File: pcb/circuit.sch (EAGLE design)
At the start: 150 parts, among them IC1 MCP73833-AMI/UN-ND, IC2 MCP3423, IC3 MCP1612-ADJI/MS, IC4 WE-TVS, IC5 ATWINC1510-MR210PB1952-ND, IC6 RN4870, IC7 MAX3378EEUD, IC8 ATSAML22N18A, J1 USB2-MICRO, J10 2.5MM-AUDIO-JACK-MONO, J11 2.5MM-AUDIO-JACK-MONO, J12 22-05-7028-02, J2 2.5MM-AUDIO-JACK-MONO, J3 2.5MM-AUDIO-JACK-MONO, J4 2.5MM-AUDIO-JACK-MONO, J5 2.5MM-AUDIO-JACK-MONO, J6 2.5MM-AUDIO-JACK-MONO, J7 2.5MM-AUDIO-JACK-MONO, J8 2.5MM-AUDIO-JACK-MONO, J9 2.5MM-AUDIO-JACK-MONO, Q1 32kHz, T1 PMOS, T10 NMOSSOT323, T11 NMOSSOT323, T12 NMOSSOT323, T13 NMOSSOT323, T2 PMOS, T3 NMOSSOT323, T4 NMOSSOT323, T5 NMOSSOT323, T6 NMOSSOT323, T7 NMOSSOT323, T8 NMOSSOT323, T9 NMOSSOT323, X1 LI-ION_BATHOL2, X2 B3S-1000, X3 MOLEX_1MM_FPC, X4 IGRID-20

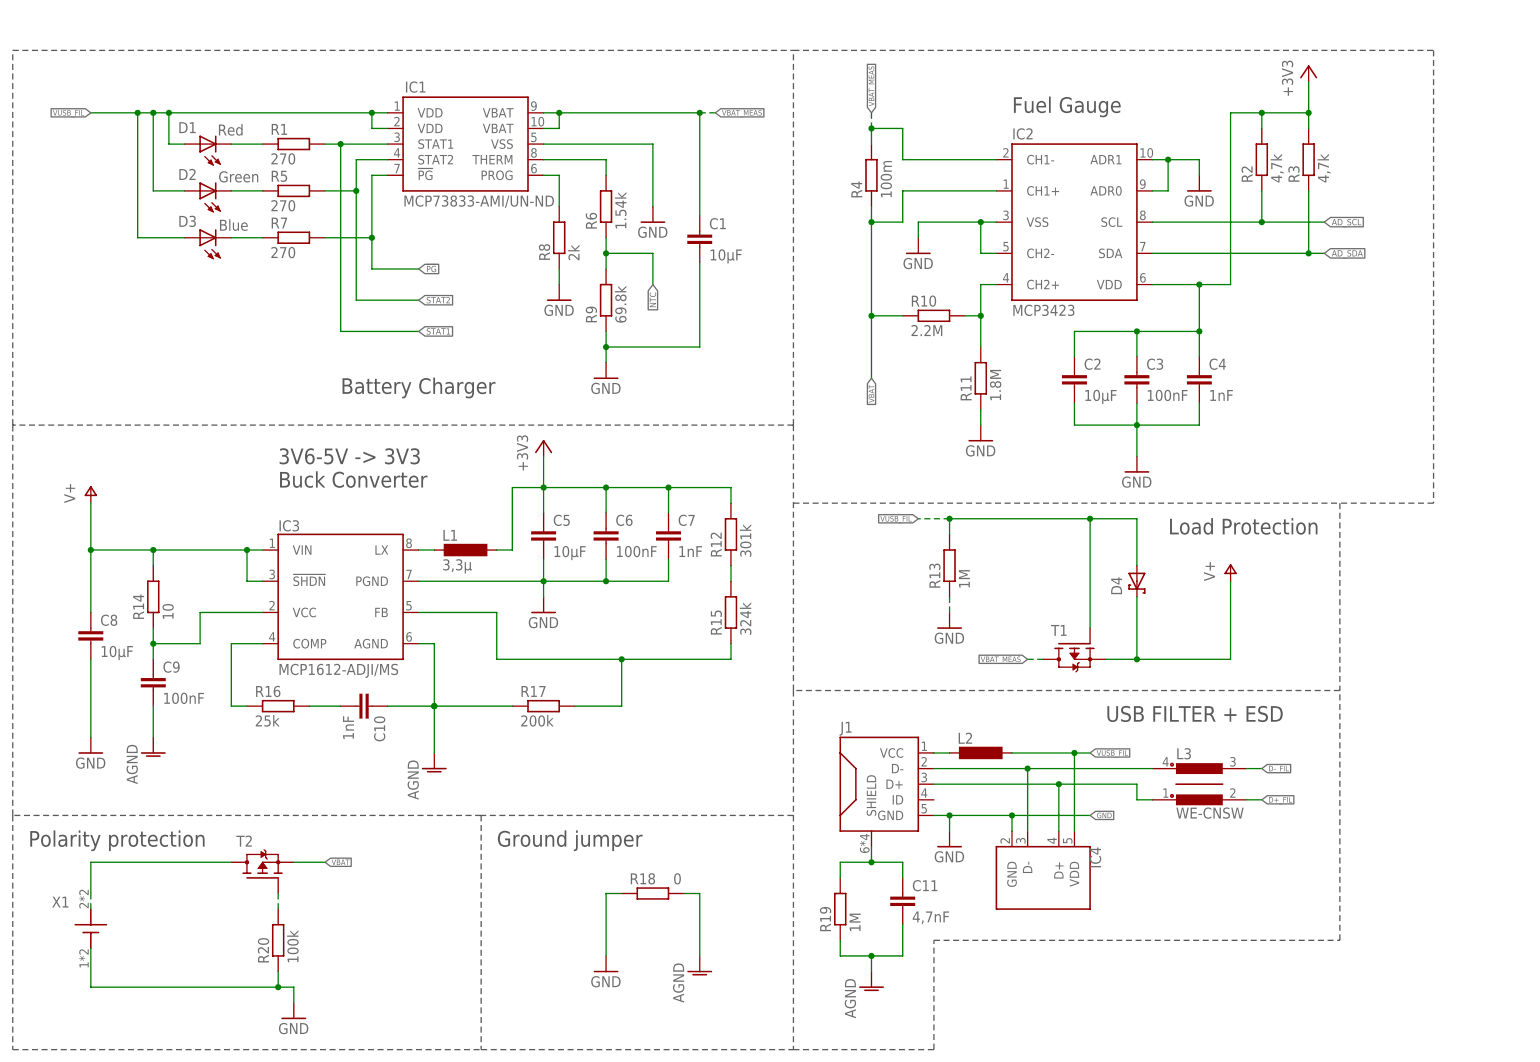
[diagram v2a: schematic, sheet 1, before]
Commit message: Board dimension created
-reworked schematics
-added PCB for battery-holder
-added PCB for UI
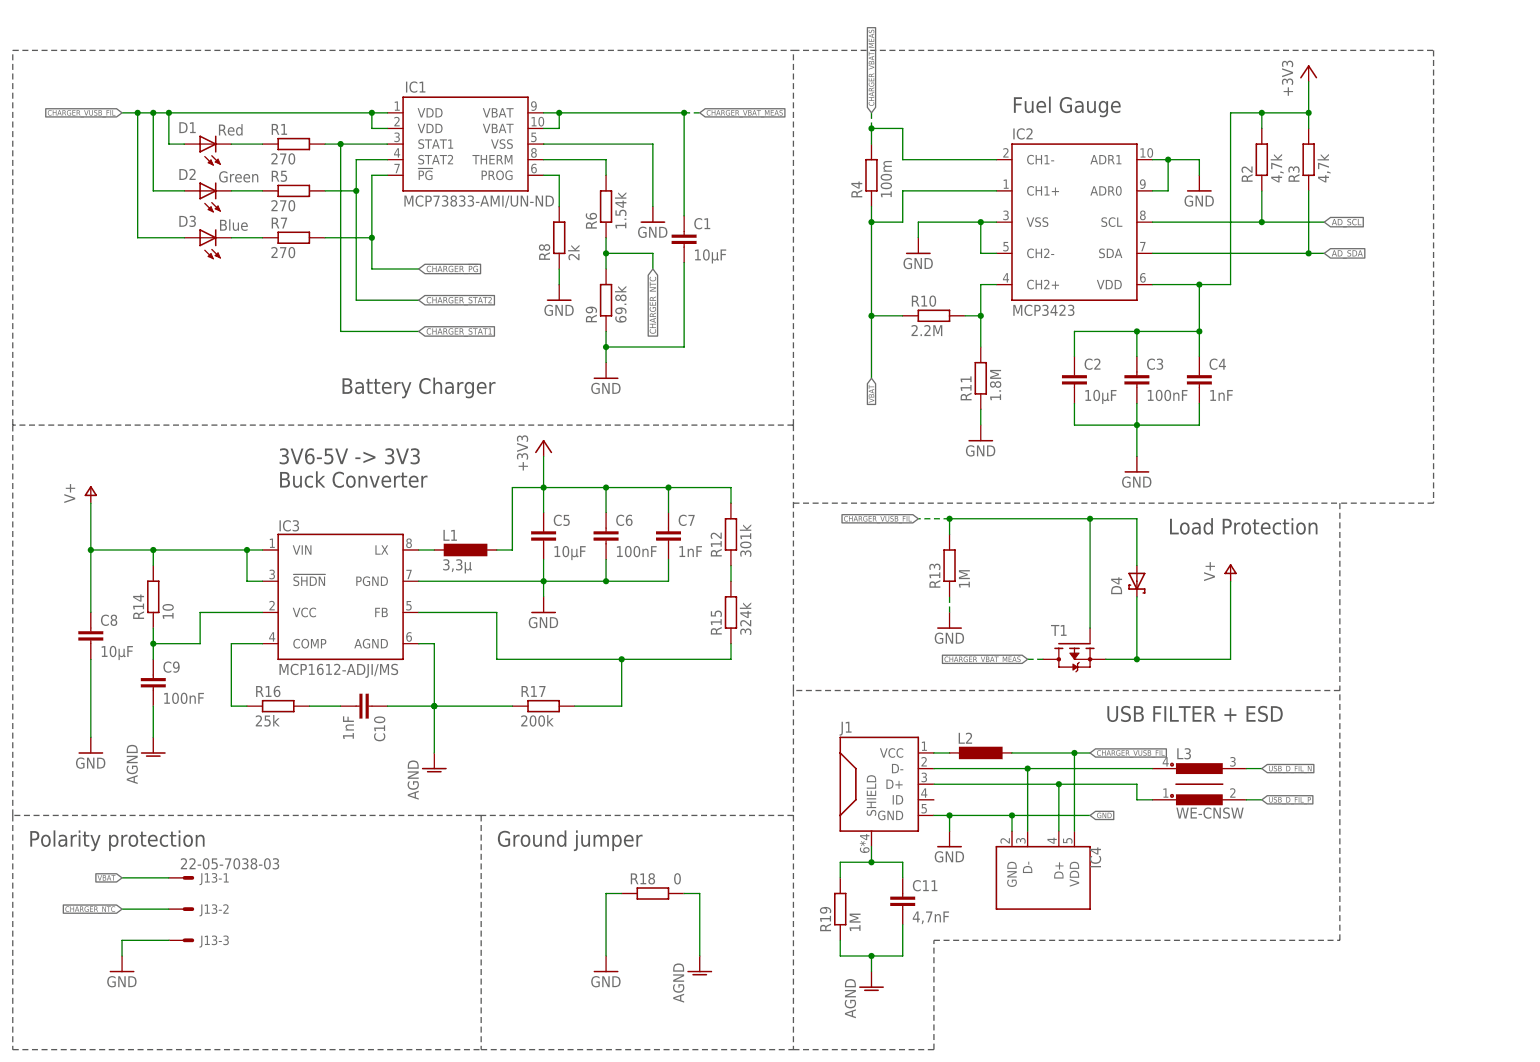
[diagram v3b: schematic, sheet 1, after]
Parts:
- removed C22: 100nF, rcl:C-EUC0603
- removed R20: 100k, rcl:R-EU_R0603
- removed T2: PMOS, thermo:PMOS
- removed X1: LI-ION_BATHOL2, thermo:LI-ION_BATHOL2
- added J13: 22-05-7038-03, con-molex:22-05-7038-03
- IC1: device Thermo_Library:MCP73833-AMI/UN-ND -> thermo:MCP73833-AMI/UN-ND; OC_MOUSER 579-MCP73833T-AMI/UN -> (none)
- IC2: OC_MOUSER 579-MCP3423-E/UN -> (none)
- IC3: OC_MOUSER 579-MCP1612T-ADJI/MS -> (none)
- IC5: device Thermo_Library:ATWINC1510-MR210PB1952-ND -> thermo:ATWINC1510-MR210PB1952-ND; OC_MOUSER 556-1510MR210UB1140 -> (none)
- IC6: device Thermo_Library:RN4870 -> thermo:RN4870; OC_MOUSER 579-RN4870-V/RM118 -> (none)
- IC8: device Thermo_Library:ATSAML22N18A -> thermo:ATSAML22N18A; OC_MOUSER 556-ATSAML22N18A-AUT -> (none)
- J11, J3, J5, J7, J9: value 2.5MM-AUDIO-JACK-MONO -> 2.5MM-AUDIO-JACK-MONONO_DRILL; device Thermo_Library:2.5MM-AUDIO-JACK-MONO -> thermo:2.5MM-AUDIO-JACK-MONONO_DRILL; OC_MOUSER 490-MJ-2523-SMT-TR -> (none)
- JP1, JP2, JP4, JP7: value (none) -> 4
- JP3: value (none) -> 3
- JP5, JP6: value (none) -> 2
- Q1: value 32kHz -> ECX-1210; device crystal:MC-405 -> thermo:ECX-1210; OC_FARNELL 2449409 -> (none)
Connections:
- net !PG! renamed CHARGER_!PG!
- net D+ renamed USB_D_P
- net D+_FIL renamed USB_D_FIL_P
- net D- renamed USB_D_N
- net D-_FIL renamed USB_D_FIL_N
- net FB renamed BUCK_FB
- net N$1 renamed AD_CH2+
- net N$12 renamed CHARGER_STAT1_LED
- net N$13 renamed BUCK_FB_R
- net N$14 renamed CHARGER_STAT2_LED
- net N$15 renamed CHARGER_!PG!_LED
- net N$16 renamed SENSOR_IN_9_DRAIN
- net N$19 renamed SENSOR_IN_0_DRAIN
- net N$2 renamed SENSOR_IN_5_DRAIN
- net N$20 renamed SENSOR_IN_1_DRAIN
- net N$21 renamed SENSOR_IN_2_DRAIN
- net N$22 renamed SENSOR_IN_3_DRAIN
- net N$24 renamed WIFI_WAKE_D
- net N$29 renamed WIFI_SPI_MISO_D
- net N$3 renamed SENSOR_IN_6_DRAIN
- net N$30 renamed WIFI_SPI_SSN_D
- net N$32 renamed OLED_EN_DRAIN
- net N$37 renamed USB_SHIELD
- net N$4 renamed SENSOR_IN_7_DRAIN
- net N$45 renamed WIFI_SPI_CFG
- net N$48 renamed WIFI_1P3V_TP
- net N$5 renamed SENSOR_IN_8_DRAIN
- net N$57 renamed BT_!RESET!
- net N$6 renamed SENSOR_IN_4_DRAIN
- net N$7 renamed !RESET!_B
- net N$8 renamed BUCK_LX
- net PROG renamed CHARGER_PROG
- net STAT1 renamed CHARGER_STAT1
- net STAT2 renamed CHARGER_STAT2
- net THERM renamed CHARGER_THERM
- net V+ renamed BUCK_V+
- net VBAT_MEAS renamed CHARGER_VBAT_MEAS
- net VUSB renamed USB_VCC
- net VUSB_FIL renamed CHARGER_VUSB_FIL
- removed net N$17: R20.2, T2.G
- removed net N$23: C18.1, C19.1, C20.1, L5.1
- removed net NTC: R6.1, R9.2
- removed net RESET: C22.1
- removed net SOF_NC: IC8.PA23
- new net +3V3_ANA: C18.1, C19.1, C20.1, IC8.VDDANA@1, IC8.VDDANA@2, L5.1
- new net CHARGER_NTC: J13-2.S, R6.1, R9.2
- net +3V3: no longer IC8.VDDANA@1, IC8.VDDANA@2
- net GND: now also J13-3.S; no longer C22.2, R20.1, X1.VBAT-
- net VBAT: now also J13-1.S; no longer T2.S
- net VIN: no longer T2.D, X1.VBAT+
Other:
- moved on the sheet: C1

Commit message: Power Unit
- placed power devices
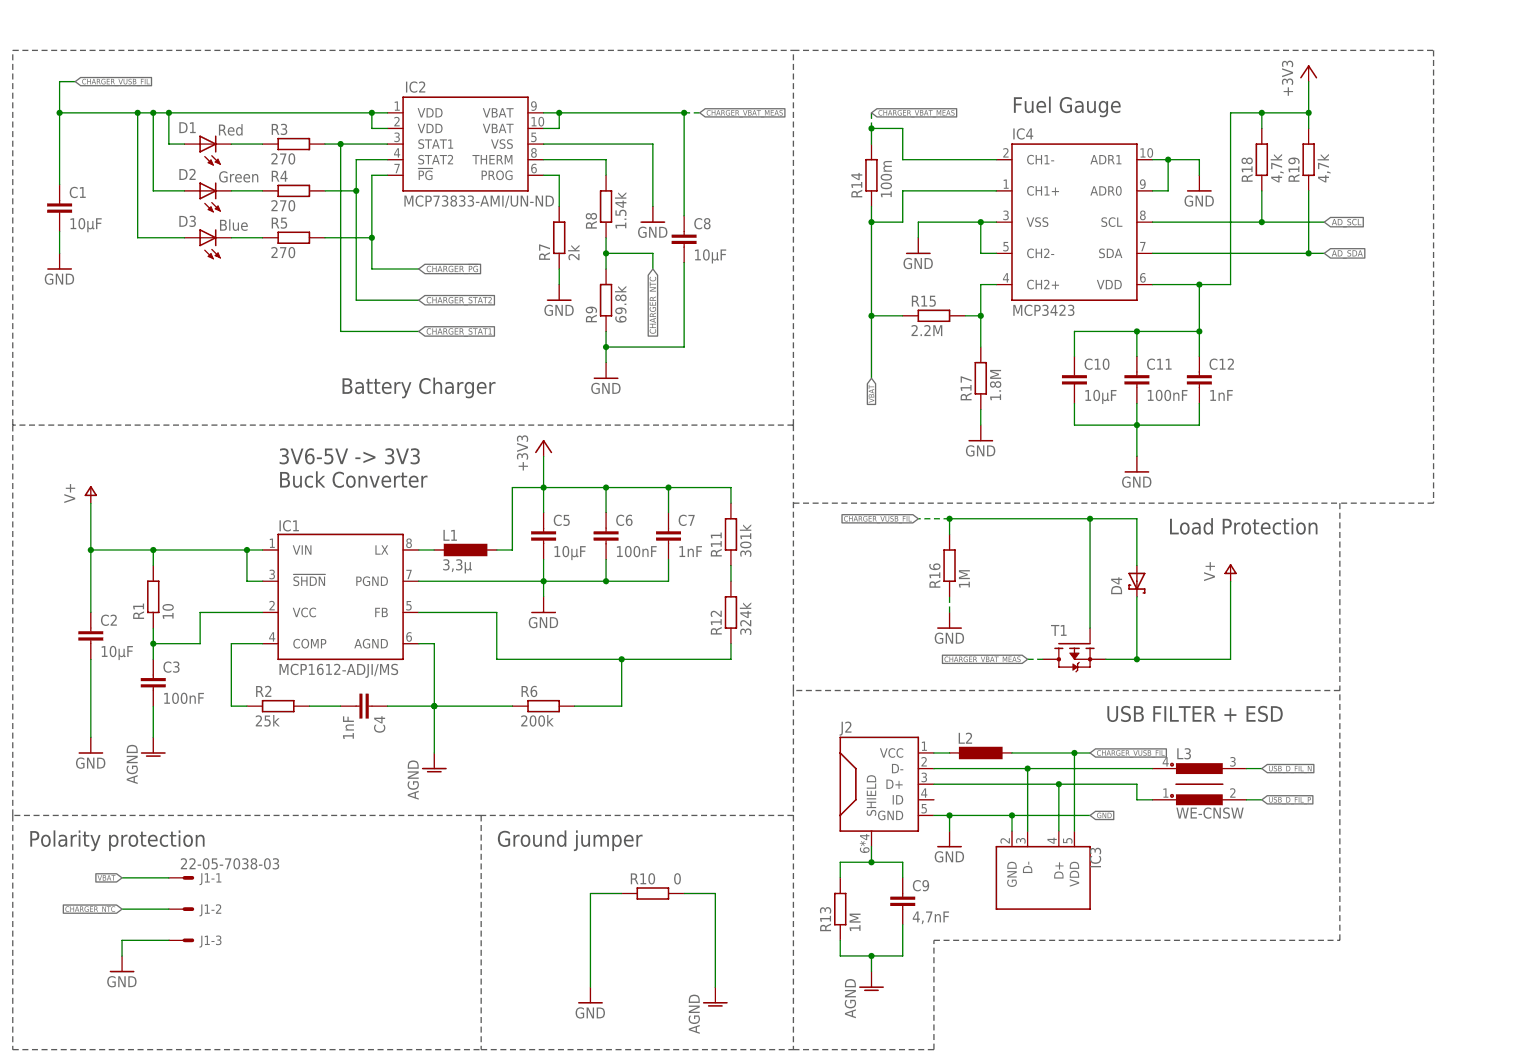
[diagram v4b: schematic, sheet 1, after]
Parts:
- removed R58: 1M, rcl:R-EU_R0603
- removed T13: NMOSSOT323, Thermo_Library:NMOSSOT323
- removed X4: IGRID-20, thermo:IGRID-20
- added C22: 10µF, rcl:C-EUC0805
- added R20: 330, rcl:R-EU_R0603
- added T2: NMOSSOT323, Thermo_Library:NMOSSOT323
- added X1: B3S-1000, Thermo_Library:B3S-1000
- C10, C27: value 1nF -> 10µF; device rcl:C-EUC0603 -> rcl:C-EUC0805; OC_MOUSER 80-C0603C102K3R -> 81-GRM21BR61E106KA3L
- C11: value 4,7nF -> 100nF; OC_MOUSER 80-C0603C472K3R -> 581-06033C104KAT2A
- C12, C28: value 100nF -> 1nF; OC_MOUSER 581-06033C104KAT2A -> 80-C0603C102K3R
- C17, C18: value 10µF -> 100nF; device rcl:C-EUC0805 -> rcl:C-EUC0603; OC_MOUSER 81-GRM21BR61E106KA3L -> 581-06033C104KAT2A
- C20, C32, C37: value 100nF -> 1µF; OC_MOUSER 581-06033C104KAT2A -> 810-CGA3E1X7R1E105AC
- C21, C34: value 100nF -> 10µF; device rcl:C-EUC0603 -> rcl:C-EUC0805; OC_MOUSER 581-06033C104KAT2A -> 81-GRM21BR61E106KA3L
- C23, C33: value 1µF -> 100nF; OC_MOUSER 810-CGA3E1X7R1E105AC -> 581-06033C104KAT2A
- C24, C25: value 22pF -> 100nF; OC_MOUSER 581-02013A220FAT2A -> 581-06033C104KAT2A
- C29: value 10µF -> 1µF; device rcl:C-EUC0805 -> rcl:C-EUC0603; OC_MOUSER 81-GRM21BR61E106KA3L -> 810-CGA3E1X7R1E105AC
- C30: value 10µF -> 1nF; device rcl:C-EUC0805 -> rcl:C-EUC0603; OC_MOUSER 81-GRM21BR61E106KA3L -> 80-C0603C102K3R
- C31: value 1nF -> 100nF; OC_MOUSER 80-C0603C102K3R -> 581-06033C104KAT2A
- C35, C36: value 1µF -> 22pF; OC_MOUSER 810-CGA3E1X7R1E105AC -> 581-02013A220FAT2A
- C9: value 100nF -> 4,7nF; OC_MOUSER 581-06033C104KAT2A -> 80-C0603C472K3R
- IC1: value MCP73833-AMI/UN-ND -> MCP1612-ADJI/MS; device thermo:MCP73833-AMI/UN-ND -> thermo:MCP1612-ADJI/MS
- IC2: value MCP3423 -> MCP73833-AMI/UN-ND; device thermo:MCP3423 -> thermo:MCP73833-AMI/UN-ND
- IC3: value MCP1612-ADJI/MS -> WE-TVS; device thermo:MCP1612-ADJI/MS -> thermo:WE-TVS; OC_MOUSER (none) -> 710-824011
- IC4: value WE-TVS -> MCP3423; device thermo:WE-TVS -> thermo:MCP3423; OC_MOUSER 710-824011 -> (none)
- IC6: value RN4870 -> MAX3378EEUD; device thermo:RN4870 -> thermo:MAX3378EEUD; OC_MOUSER (none) -> 700-MAX3378EEUD
- IC7: value MAX3378EEUD -> RN4870; device thermo:MAX3378EEUD -> thermo:RN4870; OC_MOUSER 700-MAX3378EEUD -> (none)
- J1: value USB2-MICRO -> 22-05-7038-03; device thermo:USB2-MICRO -> con-molex:22-05-7038-03; OC_MOUSER 649-10104110-0001LF -> (none)
- J10: value 2.5MM-AUDIO-JACK-MONO -> 2.5MM-AUDIO-JACK-MONONO_DRILL; device Thermo_Library:2.5MM-AUDIO-JACK-MONO -> thermo:2.5MM-AUDIO-JACK-MONONO_DRILL; OC_MOUSER 490-MJ-2523-SMT-TR -> (none)
- J12: value 22-05-7028-02 -> 2.5MM-AUDIO-JACK-MONONO_DRILL; device con-molex:22-05-7028-02 -> thermo:2.5MM-AUDIO-JACK-MONONO_DRILL; OC_MOUSER 538-22-05-7028 -> (none)
- J13: value 22-05-7038-03 -> 2.5MM-AUDIO-JACK-MONONO_DRILL; device con-molex:22-05-7038-03 -> thermo:2.5MM-AUDIO-JACK-MONONO_DRILL
- J2: value 2.5MM-AUDIO-JACK-MONO -> USB2-MICRO; device Thermo_Library:2.5MM-AUDIO-JACK-MONO -> thermo:USB2-MICRO; OC_MOUSER 490-MJ-2523-SMT-TR -> 649-10104110-0001LF
- J3, J5, J7: value 2.5MM-AUDIO-JACK-MONONO_DRILL -> 2.5MM-AUDIO-JACK-MONO; device thermo:2.5MM-AUDIO-JACK-MONONO_DRILL -> Thermo_Library:2.5MM-AUDIO-JACK-MONO; OC_MOUSER (none) -> 490-MJ-2523-SMT-TR
- J8: value 2.5MM-AUDIO-JACK-MONO -> 22-05-7028-02; device Thermo_Library:2.5MM-AUDIO-JACK-MONO -> con-molex:22-05-7028-02; OC_MOUSER 490-MJ-2523-SMT-TR -> 538-22-05-7028
- JP3: value 3 -> 2; device jumper:JP2E -> jumper:JP1E; OC_FARNELL 710-61300311121 -> (none); OC_MOUSER (none) -> 855-M20-9990246
- JP4: value 4 -> 2; device jumper:JP4E -> jumper:JP1E; OC_MOUSER 855-M20-9770446 -> 855-M20-9990246
- JP5: value 2 -> 3; device jumper:JP1E -> jumper:JP2E; OC_FARNELL (none) -> 710-61300311121; OC_MOUSER 855-M20-9990246 -> (none)
- JP6: value 2 -> 4; device jumper:JP1E -> jumper:JP4E; OC_MOUSER 855-M20-9990246 -> 855-M20-9770446
- L4: value 10µH -> L-0603; device Thermo_Library:L-1210 -> Thermo_Library:L-0603; OC_MOUSER 871-B82422H1103K -> 81-BLM18EG221SN1D
- L5: value L-0603 -> 10µH; device Thermo_Library:L-0603 -> Thermo_Library:L-1210; OC_MOUSER 81-BLM18EG221SN1D -> 871-B82422H1103K
- R1: value 270 -> 10; OC_MOUSER 652-CR0603FX-2700ELF -> 603-RC0603FR-0710RL
- R10: value 2.2M -> 0; OC_MOUSER 603-RC0603FR-072M2L -> 603-RC0603JR-070RL
- R11: value 1.8M -> 301k; OC_MOUSER 603-RC0603FR-071M8L -> 603-RC0603FR-07301KL
- R12: value 301k -> 324k; OC_MOUSER 603-RC0603FR-07301KL -> 603-RC0603FR-07324KL
- R14: value 10 -> 100m; device rcl:R-EU_R0603 -> rcl:R-EU_R5025; OC_MOUSER 603-RC0603FR-0710RL -> 652-CRM2010FXR100ELF
- R15: value 324k -> 2.2M; OC_MOUSER 603-RC0603FR-07324KL -> 603-RC0603FR-072M2L
- R16: value 25k -> 1M; device rcl:R-EU_R0805 -> rcl:R-EU_R0603; OC_MOUSER 279-CPF0805B25KE1 -> 603-RC0603FR-071ML
- R17: value 200k -> 1.8M; OC_MOUSER 603-RC0603FR-07200KL -> 603-RC0603FR-071M8L
- R18: value 0 -> 4,7k; OC_MOUSER 603-RC0603JR-070RL -> 603-RC0603FR-074K7L
- R19: value 1M -> 4,7k; OC_MOUSER 603-RC0603FR-071ML -> (none)
- R2: value 4,7k -> 25k; device rcl:R-EU_R0603 -> rcl:R-EU_R0805; OC_MOUSER 603-RC0603FR-074K7L -> 279-CPF0805B25KE1
- R21, R22: value 0 -> 1M; OC_MOUSER 603-RC0603JR-070RL -> 603-RC0603FR-071ML
- R23: value 0 -> 10k; OC_MOUSER 603-RC0603JR-070RL -> 603-RC0603FR-0710KL
- R26, R31: value 1M -> 0; OC_MOUSER 603-RC0603FR-071ML -> 603-RC0603JR-070RL
- R3: value 4,7k -> 270; OC_MOUSER (none) -> 652-CR0603FX-2700ELF
- R32: value 4,7k -> 0; OC_MOUSER (none) -> 603-RC0603JR-070RL
- R36: value 10k -> 4,7k; OC_MOUSER 603-RC0603FR-0710KL -> (none)
- R37: value 330 -> 1M; OC_MOUSER 603-RC0603FR-07330RL -> 603-RC0603FR-071ML
- R4: value 100m -> 270; device rcl:R-EU_R5025 -> rcl:R-EU_R0603; OC_FARNELL (none) -> 2447144; OC_MOUSER 652-CRM2010FXR100ELF -> (none)
- R43, R44, R45, R46, R47: value 4.7k 0.1% -> 1M; OC_MOUSER 279-CPF0603B4K7E1 -> 603-RC0603FR-071ML
- R48, R49, R50, R51, R52: value 1M -> 4.7k 0.1%; OC_MOUSER 603-RC0603FR-071ML -> 279-CPF0603B4K7E1
- R6: value 1.54k -> 200k; OC_MOUSER 660-RK73H1JTTD1541F -> 603-RC0603FR-07200KL
- R7: value 270 -> 2k; OC_FARNELL 2447144 -> (none); OC_MOUSER (none) -> 652-CR0603-FX-2001LF
- R8: value 2k -> 1.54k; OC_MOUSER 652-CR0603-FX-2001LF -> 660-RK73H1JTTD1541F
- X2: value B3S-1000 -> MOLEX_1MM_FPC; device Thermo_Library:B3S-1000 -> thermo:MOLEX_1MM_FPC; OC_MOUSER 653-B3S-1000 -> (none)
- X3: value MOLEX_1MM_FPC -> IGRID-20; device thermo:MOLEX_1MM_FPC -> thermo:IGRID-20; OC_MOUSER (none) -> 538-501645-2020
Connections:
- net !OLED_RESET: now also X3.16; no longer X4.16
- net !OLED_SPI_CS: now also X3.17; no longer X4.17
- net !PG!_TRANS: now also IC6.I/OVL1; no longer IC7.I/OVL1
- net !RESET!: now also C15.1, R20.2, R23.1; no longer C37.1, R36.1, R37.2
- net !RESET!_B: now also R20.1, X1.S; no longer R37.1, X2.S
- net +3V3: now also C10.1, C11.1, C18.1, C19.1, C20.1, C21.1, C30.1, C33.1, IC4.VDD, IC6.VL, IC7.VBAT, IC7.VDD_IO@1, IC7.VDD_IO@2, L4.2, R11.2, R18.2, R19.2, R23.2, R34.2, R35.2, X2.1, X3.2; no longer C15.1, C2.1, C26.1, C28.1, C29.1, C3.1, C35.1, C4.1, IC2.VDD, IC6.VBAT, IC6.VDD_IO@1, IC6.VDD_IO@2, IC7.VL, J10.2, J11.2, J2.2, J3.2, J4.2, J5.2, J6.2, J7.2, J8.2, J9.2, L5.2, R12.2, R2.2, R26.2, R3.2, R31.2, R32.2, X3.1, X4.2
- net +3V3_ANA: now also C22.1, C23.1, C24.1, J10.2, J11.2, J12.2, J13.2, J3.2, J4.2, J5.2, J6.2, J7.2, J9.2, L4.1; no longer C18.1, C19.1, C20.1, L5.1
- net AD_CH2+: now also IC4.CH2+, R15.2, R17.2; no longer IC2.CH2+, R10.2, R11.2
- net AD_SCL: now also IC4.SCL, JP3.1, R18.1; no longer IC2.SCL, JP5.1, R2.1
- net AD_SDA: now also IC4.SDA, JP3.2, R19.1; no longer IC2.SDA, JP5.2, R3.1
- net AGND: now also C22.2, C23.2, C24.2, C25.2, C3.2, C4.1, IC1.AGND, R10.2, R13.1, R6.1, T2.S; no longer C10.1, C11.2, C18.2, C19.2, C20.2, C21.2, IC3.AGND, R17.1, R18.2, R19.1, T12.S
- net BT_!RESET!: now also C37.1, IC7.!RST!, R36.1; no longer C33.1, IC6.!RST!, R32.1
- net BT_LINK_DROP: now also IC7.P3_2; no longer IC6.P3_2
- net BT_MODE: now also IC7.P2_0/MODE, R35.1; no longer IC6.P2_0/MODE, R31.1
- net BT_PAIRING_KEY: now also IC7.P3_4; no longer IC6.P3_4
- net BT_RSSI_IND: now also IC7.P3_1; no longer IC6.P3_1
- net BT_RX_IND: now also IC7.P3_3; no longer IC6.P3_3
- net BT_STATUS_1: now also IC7.P1_1; no longer IC6.P1_1
- net BT_STATUS_2: now also IC7.P1_0; no longer IC6.P1_0
- net BT_TX_IND: now also IC7.P2_7/TX_IND; no longer IC6.P2_7/TX_IND
- net BT_UART_CTS: now also IC7.P0_0/CTS, JP6.2; no longer IC6.P0_0/CTS, JP4.2
- net BT_UART_RTS: now also IC7.P3_6/RTS, JP6.1; no longer IC6.P3_6/RTS, JP4.1
- net BT_UART_RX: now also IC7.UART_RX, JP6.4; no longer IC6.UART_RX, JP4.4
- net BT_UART_TX: now also IC7.UART_TX, JP6.3; no longer IC6.UART_TX, JP4.3
- net BUCK_FB: now also IC1.FB, R12.1, R6.2; no longer IC3.FB, R15.1, R17.2
- net BUCK_FB_R: now also R11.1, R12.2; no longer R12.1, R15.2
- net BUCK_LX: now also IC1.LX; no longer IC3.LX
- net BUCK_RC_C: now also C4.2, R2.2; no longer C10.2, R16.2
- net BUCK_RC_R: now also IC1.COMP, R2.1; no longer IC3.COMP, R16.1
- net BUCK_V+: now also C2.1, IC1.!SHDN!, IC1.VIN, R1.2; no longer C8.1, IC3.!SHDN!, IC3.VIN, R14.2
- net BUCK_VCC: now also C3.1, IC1.VCC, R1.1; no longer C9.1, IC3.VCC, R14.1
- net CHARGER_!PG!: now also IC2.!PG, IC6.I/OVCC1, R5.2; no longer IC1.!PG, IC7.I/OVCC1, R7.2
- net CHARGER_!PG!_LED: now also R5.1; no longer R7.1
- net CHARGER_NTC: now also J1-2.S, R8.1; no longer J13-2.S, R6.1
- net CHARGER_PROG: now also IC2.PROG, R7.2; no longer IC1.PROG, R8.2
- net CHARGER_STAT1: now also IC2.STAT1, IC6.I/OVCC3, R3.2; no longer IC1.STAT1, IC7.I/OVCC3, R1.2
- net CHARGER_STAT1_LED: now also R3.1; no longer R1.1
- net CHARGER_STAT2: now also IC2.STAT2, IC6.I/OVCC2, R4.2; no longer IC1.STAT2, IC7.I/OVCC2, R5.2
- net CHARGER_STAT2_LED: now also R4.1; no longer R5.1
- net CHARGER_THERM: now also IC2.THERM, R8.2; no longer IC1.THERM, R6.2
- net CHARGER_VBAT_MEAS: now also C8.1, IC2.VBAT@1, IC2.VBAT@2, IC4.CH1-, R14.2; no longer C1.1, IC1.VBAT@1, IC1.VBAT@2, IC2.CH1-, R4.2
- net CHARGER_VUSB_FIL: now also C1.1, C32.1, IC2.VDD@1, IC2.VDD@2, IC3.VDD, IC6.!TS!, IC6.I/OVCC4, IC6.VCC, R16.2; no longer C36.1, IC1.VDD@1, IC1.VDD@2, IC4.VDD, IC7.!TS!, IC7.I/OVCC4, IC7.VCC, R13.2
- net EXT_PWM_0: now also J8-1.S; no longer J12-1.S
- net EXT_PWM_1: now also J8-2.S; no longer J12-2.S
- net GND: now also C10.2, C11.2, C18.2, C19.2, C20.2, C21.2, IC1.PGND, IC3.GND, IC4.ADR0, IC4.ADR1, IC4.CH2-, IC4.VSS, IC6.GND, IC7.GND@1, IC7.GND@2, IC7.GND@3, IC7.GND@4, IC7.GND@5, IC7.GND@6, J1-3.S, J2.GND, R10.1, R16.1, R17.1, R21.1, R22.1, R37.1, R43.1, R44.1, R45.1, R46.1, R47.1, R7.1, T12.S, X1.P, X2.6; no longer C23.2, C24.2, C25.2, C3.2, C4.2, IC1.VSS, IC2.ADR0, IC2.ADR1, IC2.CH2-, IC3.PGND, IC4.GND, IC6.GND@1, IC6.GND@2, IC6.GND@3, IC6.GND@4, IC6.GND@5, IC6.GND@6, IC7.GND, J1.GND, J13-3.S, R11.1, R13.1, R18.1, R34.1, R35.1, R48.1, R49.1, R50.1, R51.1, R52.1, R58.1, R8.1, T13.S, X2.P, X3.6
- net OLED_D/C: now also X3.4; no longer X4.4
- net OLED_EN: now also R57.2, T12.G; no longer R58.2, T13.G
- net OLED_EN_DRAIN: now also T12.D, X3.1, X3.10, X3.11, X3.12, X3.13, X3.14, X3.19, X3.20, X3.5, X3.6; no longer T13.D, X4.1, X4.10, X4.11, X4.12, X4.13, X4.14, X4.19, X4.20, X4.5, X4.6
- net OLED_SPI_MOSI: now also X3.8; no longer X4.8
- net OLED_SPI_SCLK: now also X3.7; no longer X4.7
- net RES0: now also JP5.1; no longer JP3.1
- net RES1: now also JP5.2; no longer JP3.2
- net RES2: now also JP5.3; no longer JP3.3
- net SENSOR_EN_0: now also R37.2, T2.G; no longer R48.2, T3.G
- net SENSOR_EN_1: now also R43.2, T3.G; no longer R49.2, T5.G
- net SENSOR_EN_2: now also R44.2, T4.G; no longer R50.2, T7.G
- net SENSOR_EN_3: now also R45.2, T5.G; no longer R51.2, T9.G
- net SENSOR_EN_4: now also R46.2, T6.G; no longer R52.2, T11.G
- net SENSOR_EN_5: now also R47.2, T7.G; no longer R53.2, T4.G
- net SENSOR_EN_6: now also R53.2, T8.G; no longer R54.2, T6.G
- net SENSOR_EN_7: now also R54.2, T9.G; no longer R55.2, T8.G
- net SENSOR_EN_8: now also R55.2; no longer R56.2
- net SENSOR_EN_9: now also R56.2, T11.G; no longer R57.2, T12.G
- net SENSOR_INT_0: now also J3.3; no longer J2.3
- net SENSOR_INT_2: now also J5.3; no longer J6.3
- net SENSOR_INT_3: now also J6.3; no longer J8.3
- net SENSOR_INT_4: now also J7.3; no longer J10.3
- net SENSOR_INT_5: now also J9.3; no longer J3.3
- net SENSOR_INT_6: now also J10.3; no longer J5.3
- net SENSOR_INT_7: now also J11.3; no longer J7.3
- net SENSOR_INT_8: now also J12.3; no longer J9.3
- net SENSOR_INT_9: now also J13.3; no longer J11.3
- net SENSOR_IN_0: now also J3.1; no longer J2.1
- net SENSOR_IN_0_DRAIN: now also T2.D; no longer T3.D
- net SENSOR_IN_1: now also R39.1; no longer R40.1
- net SENSOR_IN_1_DRAIN: now also R39.2, T3.D; no longer R40.2, T5.D
- net SENSOR_IN_2: now also J5.1, R40.1; no longer J6.1, R42.1
- net SENSOR_IN_2_DRAIN: now also R40.2, T4.D; no longer R42.2, T7.D
- net SENSOR_IN_3: now also J6.1, R41.1; no longer J8.1, R44.1
- net SENSOR_IN_3_DRAIN: now also R41.2, T5.D; no longer R44.2, T9.D
- net SENSOR_IN_4: now also J7.1, R42.1; no longer J10.1, R46.1
- net SENSOR_IN_4_DRAIN: now also R42.2, T6.D; no longer R46.2, T11.D
- net SENSOR_IN_5: now also J9.1, R48.1; no longer J3.1, R39.1
- net SENSOR_IN_5_DRAIN: now also R48.2, T7.D; no longer R39.2, T4.D
- net SENSOR_IN_6: now also J10.1, R49.1; no longer J5.1, R41.1
- net SENSOR_IN_6_DRAIN: now also R49.2, T8.D; no longer R41.2, T6.D
- net SENSOR_IN_7: now also J11.1, R50.1; no longer J7.1, R43.1
- net SENSOR_IN_7_DRAIN: now also R50.2, T9.D; no longer R43.2, T8.D
- net SENSOR_IN_8: now also J12.1, R51.1; no longer J9.1, R45.1
- net SENSOR_IN_8_DRAIN: now also R51.2; no longer R45.2
- net SENSOR_IN_9: now also J13.1, R52.1; no longer J11.1, R47.1
- net SENSOR_IN_9_DRAIN: now also R52.2, T11.D; no longer R47.2, T12.D
- net STAT1_TRANS: now also IC6.I/OVL3; no longer IC7.I/OVL3
- net STAT2_TRANS: now also IC6.I/OVL2; no longer IC7.I/OVL2
- net UI_BUTTON_INT_0: now also X2.2; no longer X3.2
- net UI_BUTTON_INT_1: now also X2.3; no longer X3.3
- net UI_BUTTON_INT_2: now also X2.4; no longer X3.4
- net UI_BUTTON_INT_3: now also X2.5; no longer X3.5
- net USB_CON_INT_TRANS: now also IC6.I/OVL4; no longer IC7.I/OVL4
- net USB_D_N: now also IC3.D-, J2.D-; no longer IC4.D-, J1.D-
- net USB_D_P: now also IC3.D+, J2.D+; no longer IC4.D+, J1.D+
- net USB_SHIELD: now also C9.1, J2.SHIELD, R13.2; no longer C11.1, J1.SHIELD, R19.2
- net USB_VCC: now also J2.VCC; no longer J1.VCC
- net VBAT: now also IC4.CH1+, J1-1.S, R14.1, R15.1; no longer IC2.CH1+, J13-1.S, R10.1, R4.1
- net VDDCORE: now also C25.1, C29.1, L5.2; no longer C21.1, C23.1, L4.2
- net VDDOUT: now also L5.1; no longer L4.1
- net WIFI_1P3V_TP: now also C26.1, C28.1; no longer C30.1, C32.1
- net WIFI_CHIP_EN: now also R32.1; no longer R30.1
- net WIFI_CHIP_EN_D: now also R22.2, R32.2; no longer R30.2, R35.2
- net WIFI_IRQN: now also R25.1; no longer R22.1
- net WIFI_IRQN_D: now also R25.2; no longer R22.2
- net WIFI_RESETN_D: now also R21.2; no longer R34.2
- net WIFI_SPI_CFG: now also R34.1; no longer R26.1
- net WIFI_SPI_MISO: now also R29.1; no longer R27.1
- net WIFI_SPI_MISO_D: now also R29.2; no longer R27.2
- net WIFI_SPI_MOSI: now also R27.1; no longer R24.1
- net WIFI_SPI_MOSI_D: now also R27.2; no longer R24.2
- net WIFI_SPI_SCK: now also R30.1; no longer R28.1
- net WIFI_SPI_SCK_D: now also R30.2; no longer R28.2
- net WIFI_SPI_SSN: now also R28.1; no longer R25.1
- net WIFI_SPI_SSN_D: now also R28.2; no longer R25.2
- net WIFI_UART1_RXD: now also JP4.2, R31.1; no longer JP6.2, R29.1
- net WIFI_UART1_RXD_D: now also R31.2; no longer R29.2
- net WIFI_UART1_TXD: now also JP4.1, R26.1; no longer JP6.1, R23.1
- net WIFI_UART1_TXD_D: now also R26.2; no longer R23.2
- net WIFI_WAKE: now also R24.1; no longer R21.1
- net WIFI_WAKE_D: now also R24.2; no longer R21.2
- net XIN32: now also C35.1; no longer C24.1
- net XOUT32: now also C36.1; no longer C25.1
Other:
- moved on the sheet: C1, C10, C11, C13, C14, C15, C16, C17, C18, C19, C2, C20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

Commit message: AD Converter placed
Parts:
- R21, R22: value 1M -> 0; OC_MOUSER 603-RC0603FR-071ML -> 603-RC0603JR-070RL
- R23: value 10k -> 0; OC_MOUSER 603-RC0603FR-0710KL -> 603-RC0603JR-070RL
- R31: value 0 -> 10k; OC_MOUSER 603-RC0603JR-070RL -> 603-RC0603FR-0710KL
- R32, R33: value 0 -> 1M; OC_MOUSER 603-RC0603JR-070RL -> 603-RC0603FR-071ML
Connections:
- removed net WIFI_SPI_MOSI_D: IC5.SPI_MOSI, R27.2
- removed net WIFI_UART1_TXD_D: IC5.UART_TXD, R26.2
- new net WIFI_MOSI_D: IC5.SPI_MOSI, R24.2
- new net WIFI_UART_TXD_D: IC5.UART_TXD, R23.2
- net !RESET!: now also R31.1; no longer R23.1
- net +3V3: now also R31.2; no longer R23.2
- net AD_CH2+: now also IC4.CH1+; no longer IC4.CH2+
- net CHARGER_VBAT_MEAS: now also IC4.CH2-; no longer IC4.CH1-
- net GND: now also IC4.CH1-, R32.1, R33.1; no longer IC4.CH2-, R21.1, R22.1
- net VBAT: now also IC4.CH2+; no longer IC4.CH1+
- net WIFI_CHIP_EN: now also R29.1; no longer R32.1
- net WIFI_CHIP_EN_D: now also R29.2, R33.2; no longer R22.2, R32.2
- net WIFI_IRQN: now also R22.1; no longer R25.1
- net WIFI_IRQN_D: now also R22.2; no longer R25.2
- net WIFI_RESETN: now also R30.1; no longer R33.1
- net WIFI_RESETN_D: now also R30.2, R32.2; no longer R21.2, R33.2
- net WIFI_SPI_MISO: now also R26.1; no longer R29.1
- net WIFI_SPI_MISO_D: now also R26.2; no longer R29.2
- net WIFI_SPI_MOSI: now also R24.1; no longer R27.1
- net WIFI_SPI_SCK: now also R27.1; no longer R30.1
- net WIFI_SPI_SCK_D: now also R27.2; no longer R30.2
- net WIFI_SPI_SSN: now also R25.1; no longer R28.1
- net WIFI_SPI_SSN_D: now also R25.2; no longer R28.2
- net WIFI_UART1_RXD: now also R28.1; no longer R31.1
- net WIFI_UART1_RXD_D: now also R28.2; no longer R31.2
- net WIFI_UART1_TXD: now also R23.1; no longer R26.1
- net WIFI_WAKE: now also R21.1; no longer R24.1
- net WIFI_WAKE_D: now also R21.2; no longer R24.2
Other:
- moved on the sheet: R21, R22, R23, R24, R25, R26, R27, R28, R29, R30, R31, R32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
